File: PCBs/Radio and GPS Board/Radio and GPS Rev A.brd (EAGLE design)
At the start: 95.9 x 90.2 mm, 19 parts

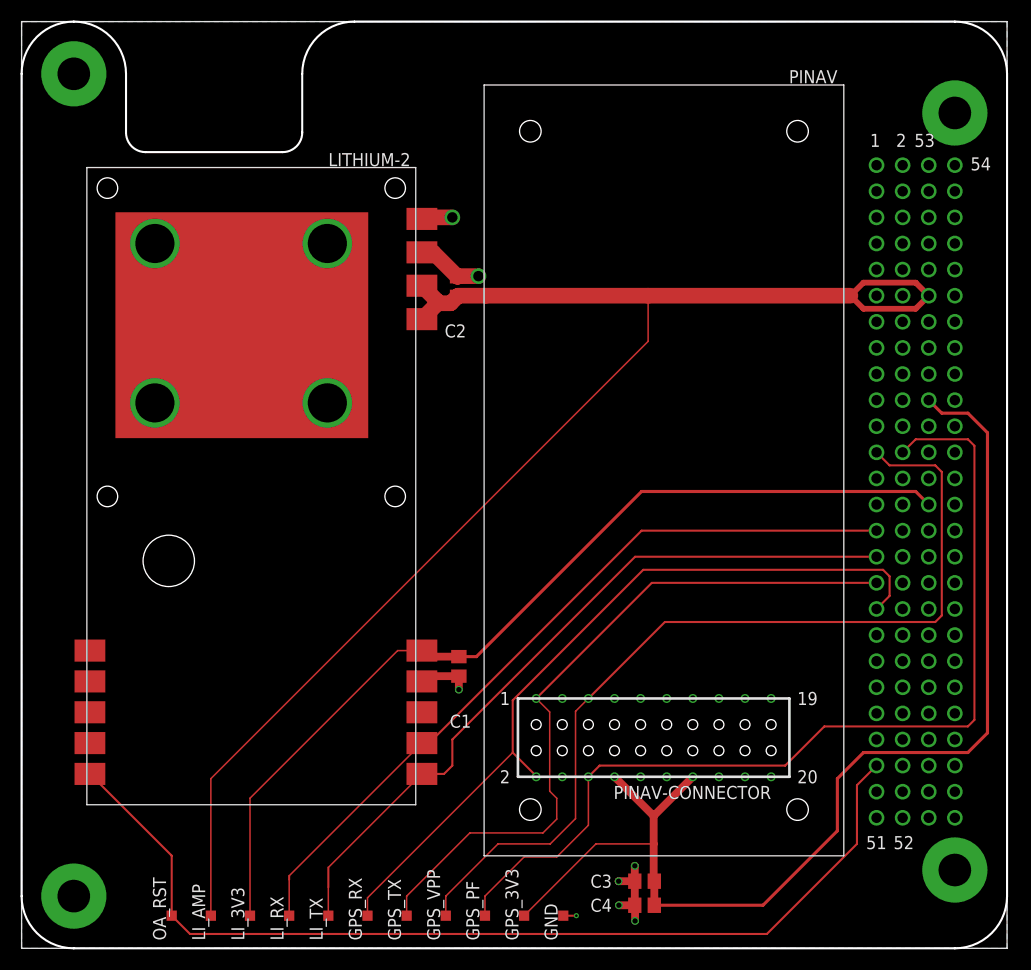
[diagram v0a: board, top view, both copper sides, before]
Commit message: Add Lithium reset pin
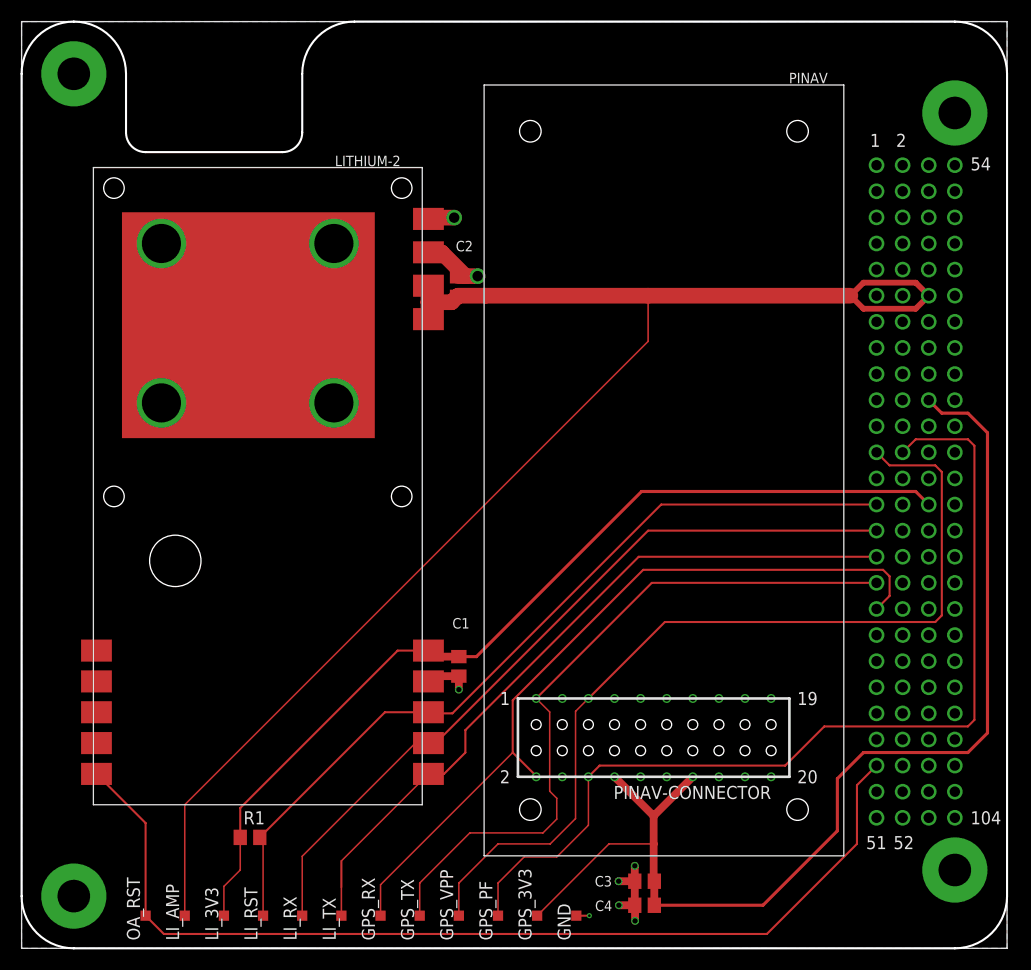
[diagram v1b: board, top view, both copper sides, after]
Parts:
- added LI_RST: TPSQTP10SQ, testpad:TP10SQ
- added R1: 47k, resistor:R0805
- moved LI_3V3 2.54 mm to (19.7, 3.17)
- moved OA_RST 2.54 mm to (12.1, 3.17)
- moved LI_AMP 2.54 mm to (15.9, 3.17)
- moved GND 1.27 mm to (54.0, 3.17)
- moved GPS_VPP 1.27 mm to (42.5, 3.17)
- moved LI_RX 1.27 mm to (27.3, 3.17)
- moved LI_TX 1.27 mm to (31.1, 3.17)
- moved GPS_3V3 1.27 mm to (50.2, 3.17)
- moved GPS_PF 1.27 mm to (46.4, 3.17)
- moved GPS_RX 1.27 mm to (34.9, 3.17)
- moved GPS_TX 1.27 mm to (38.7, 3.17)
- moved LITHIUM-2 0.64 mm to (6.99, 14.0)
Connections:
- new net LI_RST: LITHIUM-2.RESET, LI_RST.TP, R1.2, U$1.27
- net 3V3: now also R1.1
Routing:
- net LI_RST: track 0.00 -> 81.5 mm
- net SW9: track 113.6 -> 112.3 mm
- net OA_RESET: track 96.5 -> 97.8 mm
- net LI_TX: track 72.0 -> 70.9 mm
- net 3V3: track 91.5 -> 92.5 mm
- net SW3: track 140.6 -> 141.5 mm
- net GND: track 24.5 -> 23.8 mm
- net GPS_VPP: track 88.7 -> 88.2 mm
- net GPS_TX: track 70.0 -> 69.4 mm
- net GPS_RX: track 76.0 -> 75.5 mm
- net GPS_PF: track 93.8 -> 93.3 mm
